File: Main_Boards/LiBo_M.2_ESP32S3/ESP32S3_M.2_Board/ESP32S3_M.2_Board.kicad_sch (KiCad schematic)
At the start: 68 parts, among them J1 USB-C, J2 M.2-B-KEY, U1 USBLC6-2SC6, U2 TLV62568DBVR, U3 ESP32-S3R8, U4 W25Q16JVUXIQ, Y1 40MHz, Y2 32.768KHz

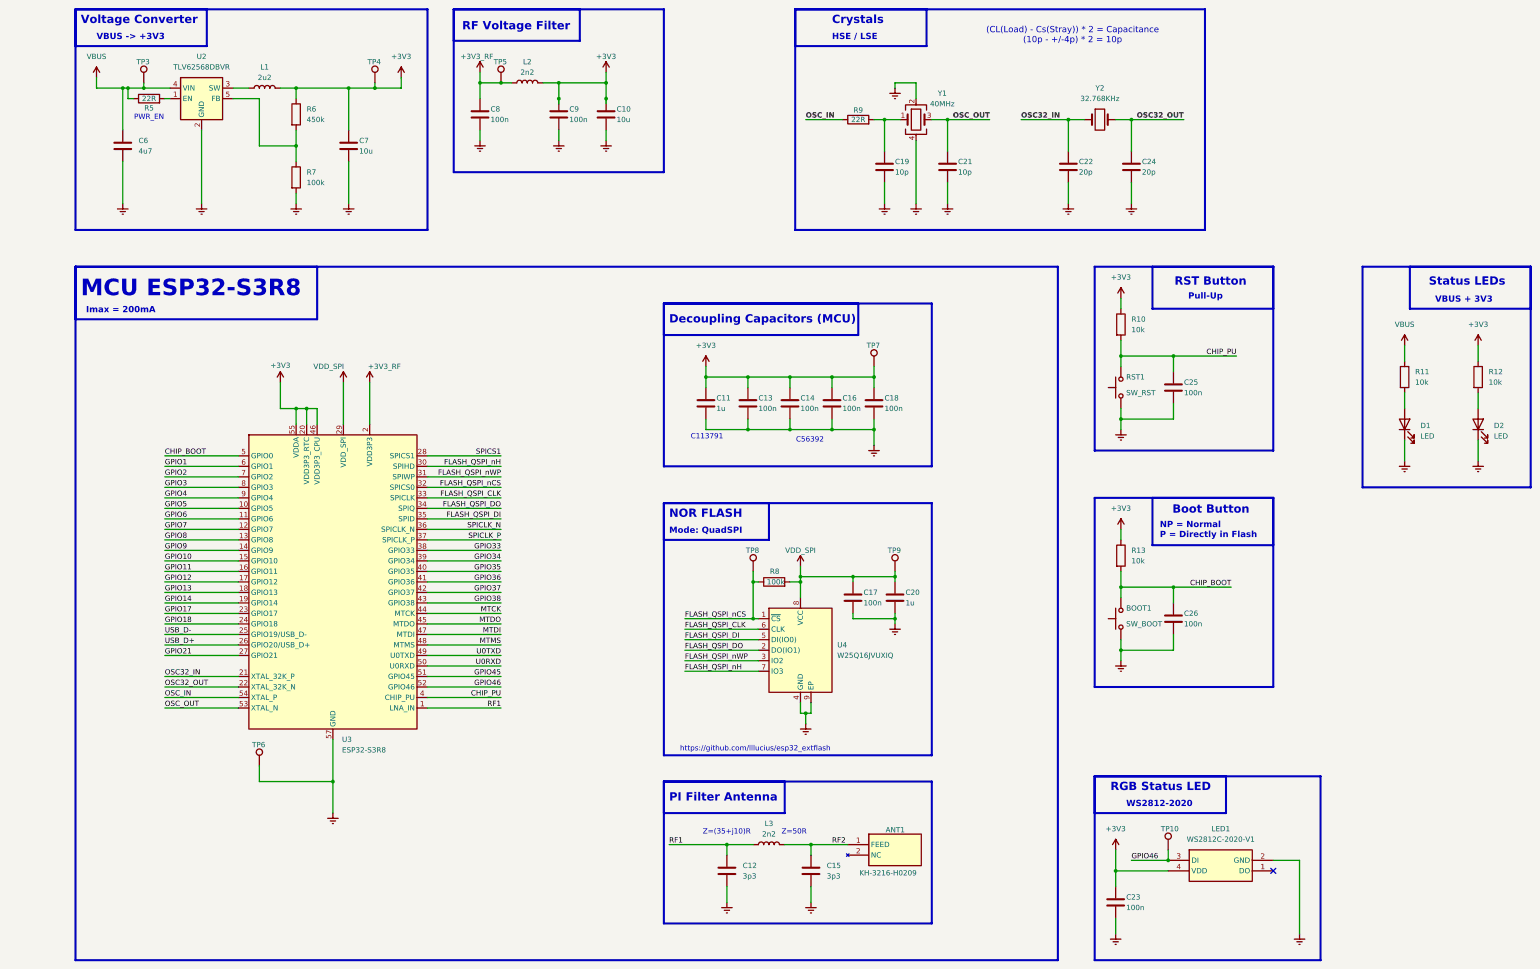
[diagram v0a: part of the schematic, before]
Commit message: Add new STEP and WRL files for M.2 Arduino and ESP32S3 Boards
- Added M.2 Arduino Module Board STEP file (12633 KB)
- Added ESP32S3 M.2 Board STEP file (16645 KB)
- Added WRL file for unnamed ESP32S3 M.2 Board (2692 KB)
- Created lock file for ESP32S3 M.2 Board project
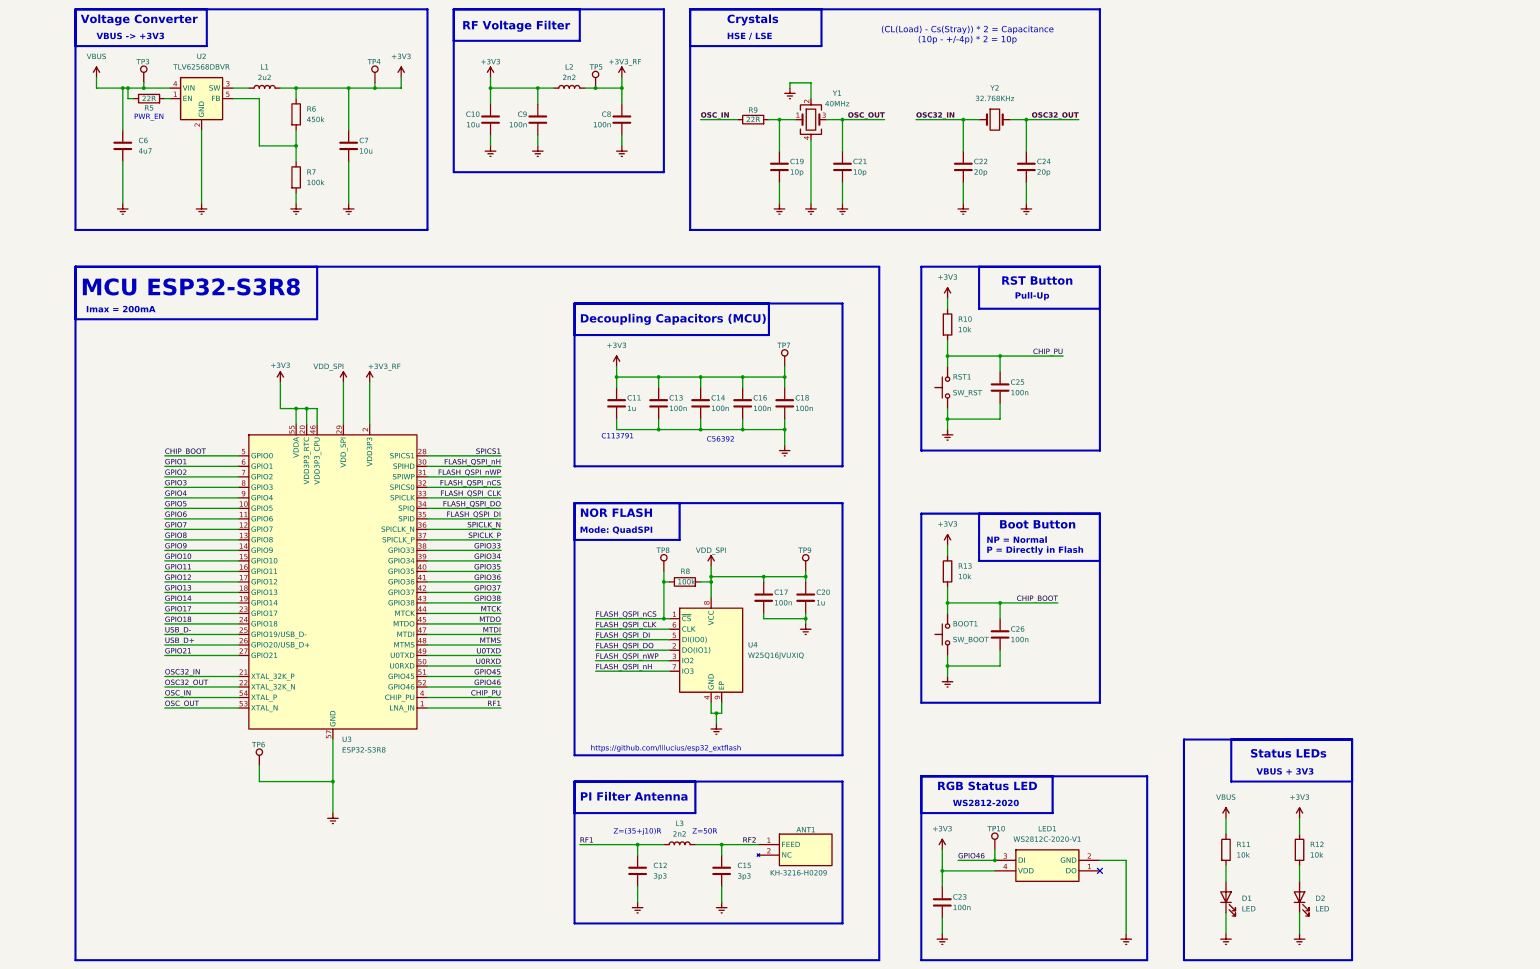
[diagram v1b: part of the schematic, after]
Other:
- moved on the sheet: ANT1, BOOT1, C10, C11, C12, C13, C14, C15, C16, C17, C18, C19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
